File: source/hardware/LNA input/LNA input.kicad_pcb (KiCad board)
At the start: 2 copper layers, 50 x 45 mm, 4 parts

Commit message: Renamed project library
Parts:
- REF** (x4): footprint Project:746600330 -> LNA input:746600330
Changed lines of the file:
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@@
 	)
 	(net 0 "")
-	(footprint "Project:746600330"
+	(footprint "LNA input:746600330"
 		(layer "B.Cu")
 		(at 165 117.5 180)
@@
 			)
 		)
-		(property "Footprint" "Project:746600330"
+		(property "Footprint" "LNA input:746600330"
 			(at 0 8 0)
 			(unlocked yes)
@@
 		)
 	)
-	(footprint "Project:746600330"
+	(footprint "LNA input:746600330"
 		(layer "B.Cu")
 		(at 125 82.5 180)
@@
 			)
 		)
-		(property "Footprint" "Project:746600330"
+		(property "Footprint" "LNA input:746600330"
 			(at 0 8 0)
 			(unlocked yes)
@@
 		)
 	)
-	(footprint "Project:746600330"
+	(footprint "LNA input:746600330"
 		(layer "B.Cu")
 		(at 165 82.5 180)
@@
 			)
 		)
-		(property "Footprint" "Project:746600330"
+		(property "Footprint" "LNA input:746600330"
 			(at 0 8 0)
 			(unlocked yes)
@@
 		)
 	)
-	(footprint "Project:746600330"
+	(footprint "LNA input:746600330"
 		(layer "B.Cu")
 		(at 125 117.5 180)
@@
 			)
 		)
-		(property "Footprint" "Project:746600330"
-			(at 0 8 0)
-			(unlocked yes)
+		(property "Footprint" "LNA input:746600330"
+			(at 0 8 0)
+			(unlocked yes)

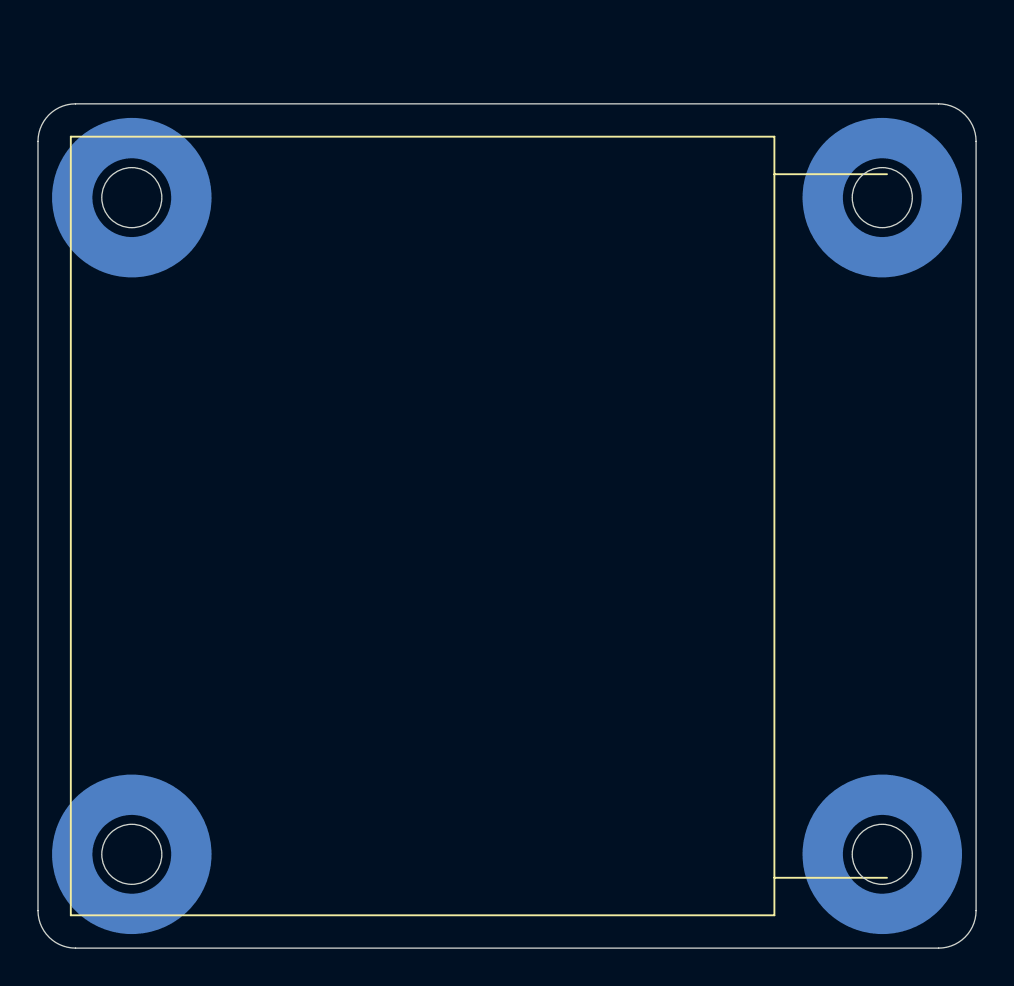
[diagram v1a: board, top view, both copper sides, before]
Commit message: Beginning of input board layout
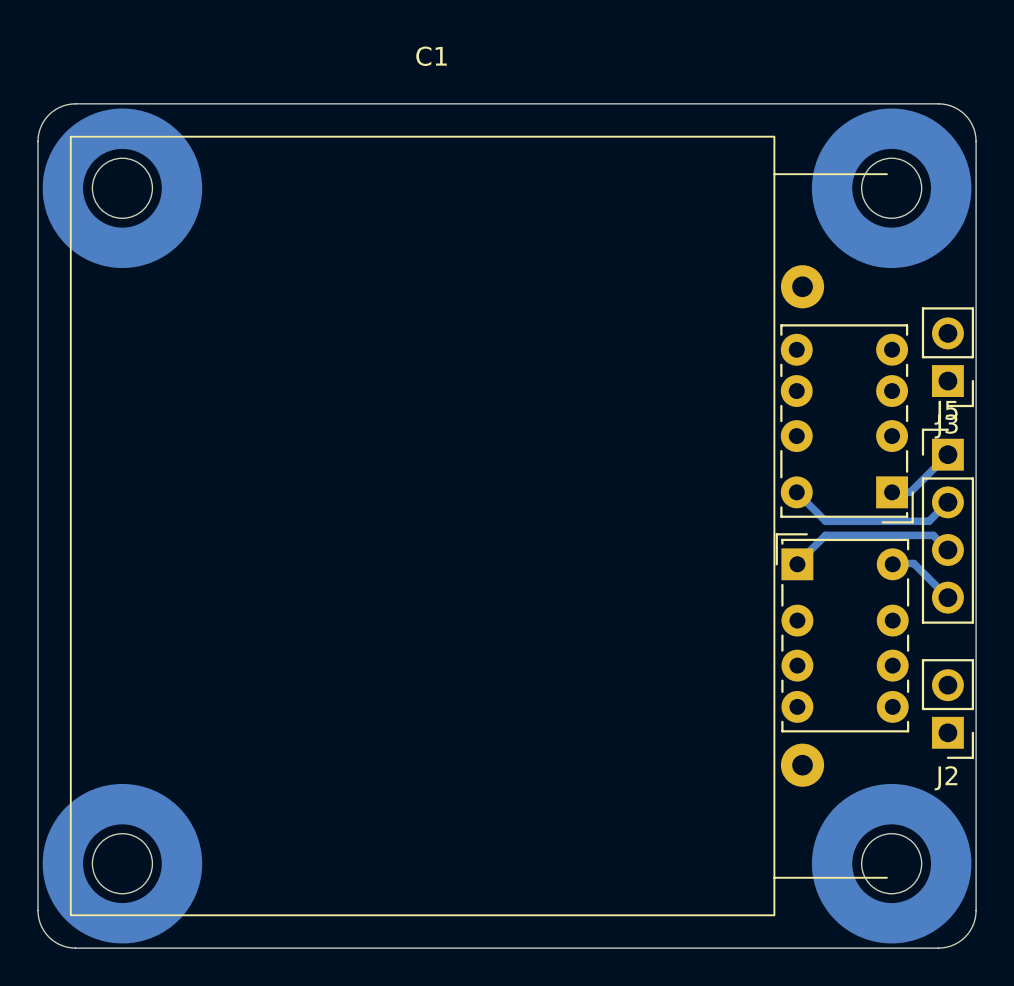
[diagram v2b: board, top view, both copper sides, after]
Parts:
- removed REF** (x4): 746600330, LNA input:746600330
- added C1: 60u, LNA input:DCP4G056007GD4KSSD flat, F.Cu at (121.8, 100.0)
- added H1: MountingHole, LNA input:746600330, B.Cu at (124.5, 82.0)
- added H2: MountingHole, LNA input:746600330, B.Cu at (165.5, 82.0)
- added H3: MountingHole, LNA input:746600330, B.Cu at (165.5, 118.0)
- added H4: MountingHole, LNA input:746600330, B.Cu at (124.5, 118.0)
- added J2: Conn_01x02, Connector_PinHeader_2.54mm:PinHeader_1x02_P2.54mm_Vertical, F.Cu at (168.5, 111.0)
- added J3: Conn_01x02, Connector_PinHeader_2.54mm:PinHeader_1x02_P2.54mm_Vertical, F.Cu at (168.5, 92.3)
- added J5: Conn_01x04, Connector_PinHeader_2.54mm:PinHeader_1x04_P2.54mm_Vertical, F.Cu at (168.5, 96.2)
- added K1: G6KU-2, Relay_THT:Relay_DPDT_Omron_G6K-2P-Y, F.Cu at (165.5, 98.2)
- added K2: G6KU-2, Relay_THT:Relay_DPDT_Omron_G6K-2P-Y, F.Cu at (160.5, 102.0)
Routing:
- net Net-(J5-Pin_2): track 0.00 -> 9.08 mm
- net Net-(J5-Pin_3): track 0.00 -> 8.97 mm
- net Net-(J5-Pin_1): track 0.00 -> 3.81 mm
- net Net-(J5-Pin_4): track 0.00 -> 3.70 mm
